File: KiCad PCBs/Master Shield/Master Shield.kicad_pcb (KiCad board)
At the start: 2 copper layers, 101.6 x 53.3 mm, 36 parts, among them J1 Power, J2 PWM, J3 Analog, J4 PWM, J5 Analog, J6 Communication

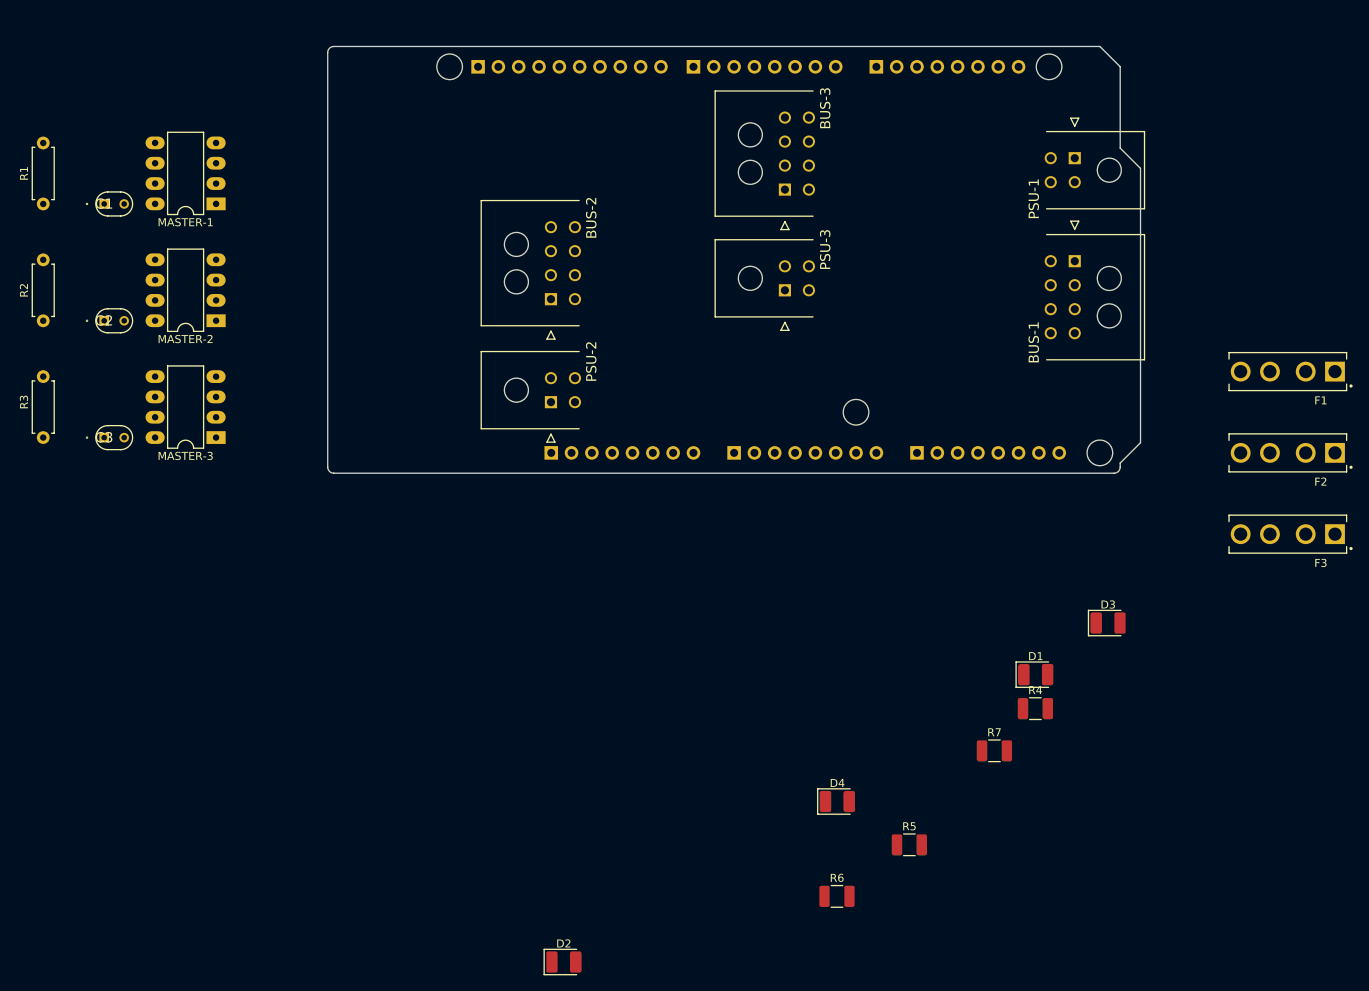
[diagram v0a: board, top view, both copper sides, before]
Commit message: Completed first version of Master Shield
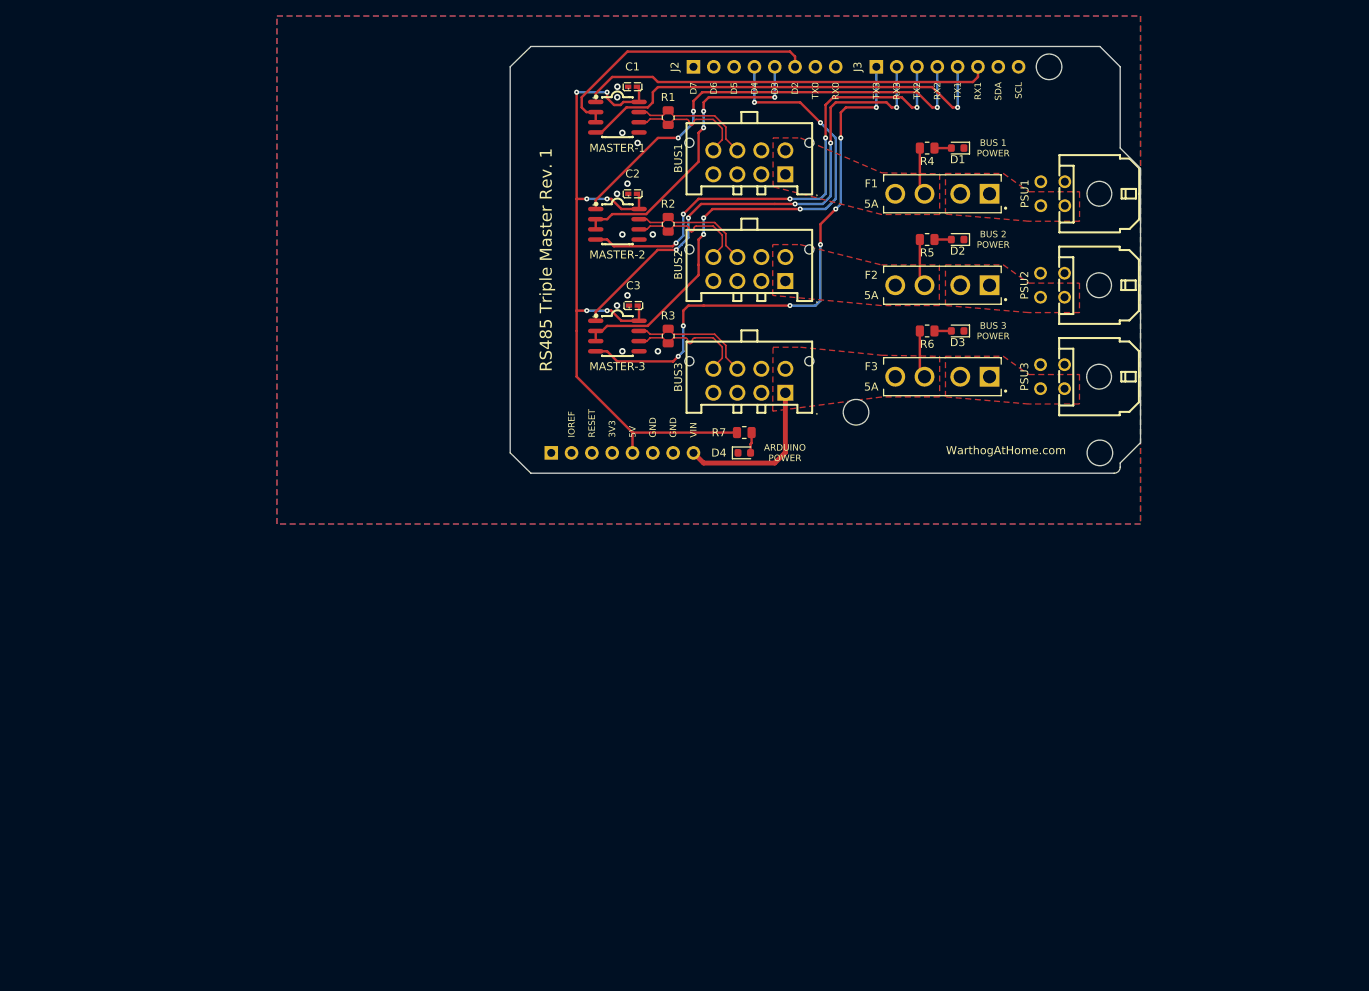
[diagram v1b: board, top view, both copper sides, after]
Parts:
- removed the J2 at (118.8, 49.2)
- removed the J3 at (150.8, 97.5)
- removed J5: Analog, Connector_PinHeader_2.54mm:PinHeader_1x08_P2.54mm_Vertical
- removed MH1: MountingHole_3.2mm, Arduino_MountingHole:MountingHole_3.2mm
- BUS1: renamed from BUS-1; footprint A10 KiCad Libraries:Molex 43045-0800 -> JLCPCB:CONN-TH_430450812
- BUS2: renamed from BUS-2; footprint A10 KiCad Libraries:Molex 43045-0800 -> JLCPCB:CONN-TH_430450812
- BUS3: renamed from BUS-3; footprint A10 KiCad Libraries:Molex 43045-0800 -> JLCPCB:CONN-TH_430450812
- C1, C2, C3: value 0.1uF -> 100n; footprint A10 KiCad Libraries:FA14 -> JLCPCB:C0402
- D1, D2, D3, D4: value GREEN -> BLUE; footprint LED_SMD:LED_1210_3225Metric_Pad1.42x2.65mm_HandSolder -> LED_SMD:LED_0603_1608Metric
- F1, F2, F3: value 6A -> 5A
- MASTER-1, MASTER-2, MASTER-3: value MAX487CPA+ -> MAX487ESA+T; footprint Package_DIP:DIP-8_W7.62mm_LongPads -> JLCPCB:SOIC-8_L5.0-W4.0-P1.27-LS6.0-BL
- PSU1: renamed from PSU-1; footprint A10 KiCad Libraries:Molex 43045-0400 -> JLCPCB:CONN-TH_0430450400
- PSU2: renamed from PSU-2; footprint A10 KiCad Libraries:Molex 43045-0400 -> JLCPCB:CONN-TH_0430450400
- PSU3: renamed from PSU-3; footprint A10 KiCad Libraries:Molex 43045-0400 -> JLCPCB:CONN-TH_0430450400
- R1, R2, R3: value 120Ω -> 120R; footprint Resistor_THT:R_Axial_DIN0207_L6.3mm_D2.5mm_P7.62mm_Horizontal -> Resistor_SMD:R_0805_2012Metric
- R4, R5, R6, R7: footprint Resistor_SMD:R_1210_3225Metric_Pad1.30x2.65mm_HandSolder -> Resistor_SMD:R_0805_2012Metric
- moved D2 102.9 mm to (178.7, 70.8), turned to 180 degrees
- moved R3 79.1 mm to (142.6, 82.9), turned to -90 degrees
- moved R2 79.0 mm to (142.6, 68.9), turned to -90 degrees
- moved R1 78.9 mm to (142.6, 55.5), turned to -90 degrees
- moved R5 75.7 mm to (174.9, 70.8), turned to 180 degrees
- moved R6 71.6 mm to (174.9, 82.2), turned to 180 degrees
- moved R4 71.4 mm to (174.9, 59.4), turned to 180 degrees
- moved PSU2 68.9 mm to (195.2, 76.5), turned to 90 degrees
- moved C3 68.2 mm to (138.2, 79.0)
- moved C2 67.9 mm to (138.1, 65.1)
- moved C1 67.6 mm to (138.1, 51.7)
- moved D1 66.5 mm to (178.7, 59.4), turned to 180 degrees
- moved MASTER-3 51.7 mm to (136.2, 82.9), turned to -90 degrees
- moved MASTER-2 51.6 mm to (136.2, 68.9), turned to -90 degrees
- moved MASTER-1 51.3 mm to (136.2, 55.5), turned to -90 degrees
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- renumbered J4 to J2, J6 to J3
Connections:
- net RS485-1-A renamed RS485-1+
- net RS485-1-B renamed RS485-1-
- net RS485-2-A renamed RS485-2+
- net RS485-2-B renamed RS485-2-
- net RS485-3-A renamed RS485-3+
- net RS485-3-B renamed RS485-3-
- BUS1 pad 1: VCC -> /12V_Fused
- BUS1 pad 5: VCC -> /12V_Fused
- BUS3 pad 1: /12V_3_Fused -> 12V_3_Fused
- BUS3 pad 5: /12V_3_Fused -> 12V_3_Fused
- D1 pad 1: unconnected-(D1-Pad1) -> GND
- D2 pad 1: unconnected-(D2-Pad1) -> GND
- D3 pad 1: unconnected-(D3-Pad1) -> GND
- F1 pad 2: VCC -> /12V_Fused
- F3 pad 2: /12V_3_Fused -> 12V_3_Fused
- J1 pad 8: VCC -> 12V_3_Fused
- R4 pad 2: VCC -> /12V_Fused
- R6 pad 2: /12V_3_Fused -> 12V_3_Fused
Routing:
- net +5V: track 0.00 -> 92.7 mm, vias 0 -> 6
- net TX3/14: track 0.00 -> 69.1 mm, vias 0 -> 7
- net *4: track 0.00 -> 66.0 mm, vias 0 -> 5
- net RX3/15: track 0.00 -> 63.0 mm, vias 0 -> 5
- net TX2/16: track 0.00 -> 61.9 mm, vias 0 -> 5
- net RX2/17: track 0.00 -> 56.9 mm, vias 0 -> 3
- net TX1/18: track 0.00 -> 54.5 mm, vias 0 -> 1
- net RX1/19: track 0.00 -> 51.5 mm
- net *3: track 0.00 -> 37.7 mm, vias 0 -> 3
- net *2: track 0.00 -> 35.1 mm
- net 12V_3_Fused: track 0.00 -> 26.0 mm
- net RS485-3-: track 0.00 -> 15.7 mm
- net RS485-2-: track 0.00 -> 15.7 mm
- net RS485-1+: track 0.00 -> 15.7 mm
- net RS485-1-: track 0.00 -> 15.7 mm
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- added copper zone on F.Cu, net +12V
- added copper zone on F.Cu, net +12V_2
- added copper zone on F.Cu, net +12V_3
- added copper zone on F.Cu, net /12V_2_Fused
- added copper zone on F.Cu, net /12V_Fused
- added copper zone on F.Cu, net 12V_3_Fused
- added copper zone on B.Cu, net GND
- added copper zone on F.Cu, net GND
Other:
- board size 101.6 x 53.3 mm -> 78.8 x 53.3 mm
- board text added: "3V3"
- board text added: "5V"
- board text added: "ARDUINO POWER"
- board text added: "BRRRRRRRRRRRT"
- board text added: "BUS 1 POWER"
- board text added: "BUS 2 POWER"
- board text added: "BUS 3 POWER"
- board text added: "D2"
- board text added: "D3"
- board text added: "D4"
- board text added: "D5"
- board text added: "D6"
- board text added: "D7"
- board text added: "GND"
- board text added: "IOREF"
- board text added: "RESET"
- board text added: "RS485 Triple Master Rev. 1"
- board text added: "RX0"
- board text added: "RX1"
- board text added: "RX2"
- board text added: "RX3"
- board text added: "SCL"
- board text added: "SDA"
- board text added: "TX0"
- board text added: "TX1"
- board text added: "TX2"
- board text added: "TX3"
- board text added: "This is a shield, the pin headers must be facing down."
- board text added: "VIN"
- board text added: "WarthogAtHome.com"
